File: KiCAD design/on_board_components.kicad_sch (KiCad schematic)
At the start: 11 parts, among them U401 ACS712xLCTR-20A

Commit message: add some comments, connector for battery, bluetooth (is now the PMOD BLE from digikey)
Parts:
- D401: Price 0,35 -> 0.35
- D402, D403: Price 0,36 -> 0.36
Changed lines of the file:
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@@
       (effects (font (size 1.27 1.27)) hide)
     )
-    (property "Price" "0,35" (id 5) (at 133.35 50.8 90)
+    (property "Price" "0.35" (id 5) (at 133.35 50.8 90)
       (effects (font (size 1.27 1.27)) hide)
     )
@@
       (effects (font (size 1.27 1.27)) hide)
     )
-    (property "Price" "0,36" (id 5) (at 162.56 54.61 90)
+    (property "Price" "0.36" (id 5) (at 162.56 54.61 90)
       (effects (font (size 1.27 1.27)) hide)
     )
@@
       (effects (font (size 1.27 1.27)) hide)
     )
-    (property "Price" "0,36" (id 5) (at 176.53 54.61 90)
+    (property "Price" "0.36" (id 5) (at 176.53 54.61 90)
       (effects (font (size 1.27 1.27)) hide)
     )

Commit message: Added capacitors and resistors
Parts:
- C401, C402: footprint Capacitor_SMD:C_0603_1608Metric_Pad1.08x0.95mm_HandSolder -> Capacitor_SMD:C_0805_2012Metric; Price (none) -> 0,09; PurchaseLoc (none) -> https://www.digikey.fi/fi/products/detail/yageo/CC0805KRX7R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
- R404, R405: footprint Resistor_SMD:R_0603_1608Metric_Pad0.98x0.95mm_HandSolder -> Resistor_SMD:R_0805_2012Metric; Price (none) -> 0,09; PurchaseLoc (none) -> https://www.digikey.fi/fi/products/detail/yageo/RC0805FR-07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
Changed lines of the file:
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@@
       (effects (font (size 1.27 1.27)) (justify right))
     )
-    (property "Footprint" "Capacitor_SMD:C_0603_1608Metric_Pad1.08x0.95mm_HandSolder" (id 2) (at 45.4152 31.75 0)
-      (effects (font (size 1.27 1.27)) hide)
-    )
-    (property "Datasheet" "~" (id 3) (at 44.45 35.56 0)
+    (property "Footprint" "Capacitor_SMD:C_0805_2012Metric" (id 2) (at 45.4152 31.75 0)
+      (effects (font (size 1.27 1.27)) hide)
+    )
+    (property "Datasheet" "https://www.yageo.com/upload/media/product/productsearch/datasheet/mlcc/UPY-GPHC_X7R_6.3V-to-250V_22.pdf" (id 3) (at 44.45 35.56 0)
+      (effects (font (size 1.27 1.27)) hide)
+    )
+    (property "PurchaseLoc" "https://www.digikey.fi/fi/products/detail/yageo/CC0805KRX7R9BB104/302874" (id 4) (at 44.45 35.56 0)
+      (effects (font (size 1.27 1.27)) hide)
+    )
+    (property "Price" "0,09" (id 5) (at 44.45 35.56 0)
       (effects (font (size 1.27 1.27)) hide)
     )
@@
       (effects (font (size 1.27 1.27)) (justify right))
     )
-    (property "Footprint" "Capacitor_SMD:C_0603_1608Metric_Pad1.08x0.95mm_HandSolder" (id 2) (at 66.3448 63.5 0)
-      (effects (font (size 1.27 1.27)) hide)
-    )
-    (property "Datasheet" "~" (id 3) (at 67.31 67.31 0)
+    (property "Footprint" "Capacitor_SMD:C_0805_2012Metric" (id 2) (at 66.3448 63.5 0)
+      (effects (font (size 1.27 1.27)) hide)
+    )
+    (property "Datasheet" "https://www.yageo.com/upload/media/product/productsearch/datasheet/mlcc/UPY-GPHC_X7R_6.3V-to-250V_22.pdf" (id 3) (at 67.31 67.31 0)
+      (effects (font (size 1.27 1.27)) hide)
+    )
+    (property "PurchaseLoc" "https://www.digikey.fi/fi/products/detail/yageo/CC0805KRX7R9BB102/302861" (id 4) (at 67.31 67.31 0)
+      (effects (font (size 1.27 1.27)) hide)
+    )
+    (property "Price" "0,09" (id 5) (at 67.31 67.31 0)
       (effects (font (size 1.27 1.27)) hide)
     )
@@
       (effects (font (size 1.27 1.27)) (justify left))
     )
-    (property "Footprint" "Resistor_SMD:R_0603_1608Metric_Pad0.98x0.95mm_HandSolder" (id 2) (at 81.28 60.96 0)
-      (effects (font (size 1.27 1.27)) hide)
-    )
-    (property "Datasheet" "~" (id 3) (at 81.28 60.96 0)
+    (property "Footprint" "Resistor_SMD:R_0805_2012Metric" (id 2) (at 81.28 60.96 0)
+      (effects (font (size 1.27 1.27)) hide)
+    )
+    (property "Datasheet" "https://www.yageo.com/upload/media/product/productsearch/datasheet/rchip/PYu-RC_Group_51_RoHS_L_12.pdf" (id 3) (at 81.28 60.96 0)
+      (effects (font (size 1.27 1.27)) hide)
+    )
+    (property "PurchaseLoc" "https://www.digikey.fi/fi/products/detail/yageo/RC0805FR-071KL/727444" (id 4) (at 81.28 60.96 0)
+      (effects (font (size 1.27 1.27)) hide)
+    )
+    (property "Price" "0,09" (id 5) (at 81.28 60.96 0)
       (effects (font (size 1.27 1.27)) hide)
     )
@@
       (effects (font (size 1.27 1.27)) (justify left))
     )
-    (property "Footprint" "Resistor_SMD:R_0603_1608Metric_Pad0.98x0.95mm_HandSolder" (id 2) (at 81.28 71.12 0)
-      (effects (font (size 1.27 1.27)) hide)
-    )
-    (property "Datasheet" "~" (id 3) (at 81.28 71.12 0)
-      (effects (font (size 1.27 1.27)) hide)
-    )
+    (property "Footprint" "Resistor_SMD:R_0805_2012Metric" (id 2) (at 81.28 71.12 0)
+      (effects (font (size 1.27 1.27)) hide)
+    )
+    (property "Datasheet" "https://www.yageo.com/upload/media/product/productsearch/datasheet/rchip/PYu-RC_Group_51_RoHS_L_12.pdf" (id 3) (at 81.28 71.12 0)
+      (effects (font (size 1.27 1.27)) hide)
+    )
+    (property "PurchaseLoc" "https://www.digikey.fi/fi/products/detail/yageo/RC0805FR-071K91L/727529" (id 4) (at 81.28 71.12 0)
+      (effects (font (size 1.27 1.27)) hide)
+    )
+    (property "Price" "0,09" (id 5) (at 81.28 71.12 0)
+      (effects (font (size 1.27 1.27)) hide)
+    )

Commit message: add link to switch and 1k resistor
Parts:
- R401, R402, R403: Price (none) -> 0.27; PurchaseLoc (none) -> https://www.digikey.fi/fi/products/detail/stackpole-electro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
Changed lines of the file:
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@@
+      (effects (font (size 1.27 1.27)) hide)
+    )
+    (property "Price" "0.27" (id 4) (at 176.53 62.23 0)
+      (effects (font (size 1.27 1.27)) hide)
+    )
+    (property "PurchaseLoc" "https://www.digikey.fi/fi/products/detail/stackpole-electronics-inc/RNCP0805FTD1K00/2240229" (id 5) (at 176.53 62.23 0)
       (effects (font (size 1.27 1.27)) hide)
     )
@@
       (effects (font (size 1.27 1.27)) hide)
     )
+    (property "Price" "0.27" (id 4) (at 162.56 62.23 0)
+      (effects (font (size 1.27 1.27)) hide)
+    )
+    (property "PurchaseLoc" "https://www.digikey.fi/fi/products/detail/stackpole-electronics-inc/RNCP0805FTD1K00/2240229" (id 5) (at 162.56 62.23 0)
+      (effects (font (size 1.27 1.27)) hide)
+    )
     (pin "1")
     (pin "2")
@@
       (effects (font (size 1.27 1.27)) hide)
     )
+    (property "Price" "0.27" (id 4) (at 133.35 58.42 0)
+      (effects (font (size 1.27 1.27)) hide)
+    )
+    (property "PurchaseLoc" "https://www.digikey.fi/fi/products/detail/stackpole-electronics-inc/RNCP0805FTD1K00/2240229" (id 5) (at 133.35 58.42 0)
+      (effects (font (size 1.27 1.27)) hide)
+    )

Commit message: use . as decimal separator
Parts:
- C401, C402, R404, R405: Price 0,09 -> 0.09
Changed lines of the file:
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@@
       (effects (font (size 1.27 1.27)) hide)
     )
-    (property "Price" "0,09" (id 5) (at 44.45 35.56 0)
+    (property "Price" "0.09" (id 5) (at 44.45 35.56 0)
       (effects (font (size 1.27 1.27)) hide)
     )
@@
       (effects (font (size 1.27 1.27)) hide)
     )
-    (property "Price" "0,09" (id 5) (at 67.31 67.31 0)
+    (property "Price" "0.09" (id 5) (at 67.31 67.31 0)
       (effects (font (size 1.27 1.27)) hide)
     )
@@
       (effects (font (size 1.27 1.27)) hide)
     )
-    (property "Price" "0,09" (id 5) (at 81.28 60.96 0)
+    (property "Price" "0.09" (id 5) (at 81.28 60.96 0)
       (effects (font (size 1.27 1.27)) hide)
     )
@@
       (effects (font (size 1.27 1.27)) hide)
     )
-    (property "Price" "0,09" (id 5) (at 81.28 71.12 0)
-      (effects (font (size 1.27 1.27)) hide)
-    )
+    (property "Price" "0.09" (id 5) (at 81.28 71.12 0)
+      (effects (font (size 1.27 1.27)) hide)
+    )

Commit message: Fixed info of 3 resistors in LED sheet
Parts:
- R401, R402, R403: footprint Resistor_SMD:R_0603_1608Metric_Pad0.98x0.95mm_HandSolder -> Resistor_SMD:R_0805_2012Metric; Price 0.27 -> 0.09; PurchaseLoc https://www.digikey.fi/fi/products/detail/stackpole-electro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 -> https://www.digikey.fi/fi/products/detail/yageo/RC0805FR-07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
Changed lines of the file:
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@@
       (effects (font (size 1.27 1.27)) (justify left))
     )
-    (property "Footprint" "Resistor_SMD:R_0603_1608Metric_Pad0.98x0.95mm_HandSolder" (id 2) (at 176.53 62.23 0)
-      (effects (font (size 1.27 1.27)) hide)
-    )
-    (property "Datasheet" "~" (id 3) (at 176.53 62.23 0)
-      (effects (font (size 1.27 1.27)) hide)
-    )
-    (property "Price" "0.27" (id 4) (at 176.53 62.23 0)
-      (effects (font (size 1.27 1.27)) hide)
-    )
-    (property "PurchaseLoc" "https://www.digikey.fi/fi/products/detail/stackpole-electronics-inc/RNCP0805FTD1K00/2240229" (id 5) (at 176.53 62.23 0)
+    (property "Footprint" "Resistor_SMD:R_0805_2012Metric" (id 2) (at 176.53 62.23 0)
+      (effects (font (size 1.27 1.27)) hide)
+    )
+    (property "Datasheet" "https://www.yageo.com/upload/media/product/productsearch/datasheet/rchip/PYu-RC_Group_51_RoHS_L_12.pdf" (id 3) (at 176.53 62.23 0)
+      (effects (font (size 1.27 1.27)) hide)
+    )
+    (property "Price" "0.09" (id 4) (at 176.53 62.23 0)
+      (effects (font (size 1.27 1.27)) hide)
+    )
+    (property "PurchaseLoc" "https://www.digikey.fi/fi/products/detail/yageo/RC0805FR-071KL/727444" (id 5) (at 176.53 62.23 0)
       (effects (font (size 1.27 1.27)) hide)
     )
@@
       (effects (font (size 1.27 1.27)) (justify left))
     )
-    (property "Footprint" "Resistor_SMD:R_0603_1608Metric_Pad0.98x0.95mm_HandSolder" (id 2) (at 162.56 62.23 0)
-      (effects (font (size 1.27 1.27)) hide)
-    )
-    (property "Datasheet" "~" (id 3) (at 162.56 62.23 0)
-      (effects (font (size 1.27 1.27)) hide)
-    )
-    (property "Price" "0.27" (id 4) (at 162.56 62.23 0)
-      (effects (font (size 1.27 1.27)) hide)
-    )
-    (property "PurchaseLoc" "https://www.digikey.fi/fi/products/detail/stackpole-electronics-inc/RNCP0805FTD1K00/2240229" (id 5) (at 162.56 62.23 0)
+    (property "Footprint" "Resistor_SMD:R_0805_2012Metric" (id 2) (at 162.56 62.23 0)
+      (effects (font (size 1.27 1.27)) hide)
+    )
+    (property "Datasheet" "https://www.yageo.com/upload/media/product/productsearch/datasheet/rchip/PYu-RC_Group_51_RoHS_L_12.pdf" (id 3) (at 162.56 62.23 0)
+      (effects (font (size 1.27 1.27)) hide)
+    )
+    (property "Price" "0.09" (id 4) (at 162.56 62.23 0)
+      (effects (font (size 1.27 1.27)) hide)
+    )
+    (property "PurchaseLoc" "https://www.digikey.fi/fi/products/detail/yageo/RC0805FR-071KL/727444" (id 5) (at 162.56 62.23 0)
       (effects (font (size 1.27 1.27)) hide)
     )
@@
       (effects (font (size 1.27 1.27)) (justify left))
     )
-    (property "Footprint" "Resistor_SMD:R_0603_1608Metric_Pad0.98x0.95mm_HandSolder" (id 2) (at 133.35 58.42 0)
-      (effects (font (size 1.27 1.27)) hide)
-    )
-    (property "Datasheet" "~" (id 3) (at 133.35 58.42 0)
-      (effects (font (size 1.27 1.27)) hide)
-    )
-    (property "Price" "0.27" (id 4) (at 133.35 58.42 0)
-      (effects (font (size 1.27 1.27)) hide)
-    )
-    (property "PurchaseLoc" "https://www.digikey.fi/fi/products/detail/stackpole-electronics-inc/RNCP0805FTD1K00/2240229" (id 5) (at 133.35 58.42 0)
-      (effects (font (size 1.27 1.27)) hide)
-    )
+    (property "Footprint" "Resistor_SMD:R_0805_2012Metric" (id 2) (at 133.35 58.42 0)
+      (effects (font (size 1.27 1.27)) hide)
+    )
+    (property "Datasheet" "https://www.yageo.com/upload/media/product/productsearch/datasheet/rchip/PYu-RC_Group_51_RoHS_L_12.pdf" (id 3) (at 133.35 58.42 0)
+      (effects (font (size 1.27 1.27)) hide)
+    )
+    (property "Price" "0.09" (id 4) (at 133.35 58.42 0)
+      (effects (font (size 1.27 1.27)) hide)
+    )
+    (property "PurchaseLoc" "https://www.digikey.fi/fi/products/detail/yageo/RC0805FR-071KL/727444" (id 5) (at 133.35 58.42 0)
+      (effects (font (size 1.27 1.27)) hide)
+    )

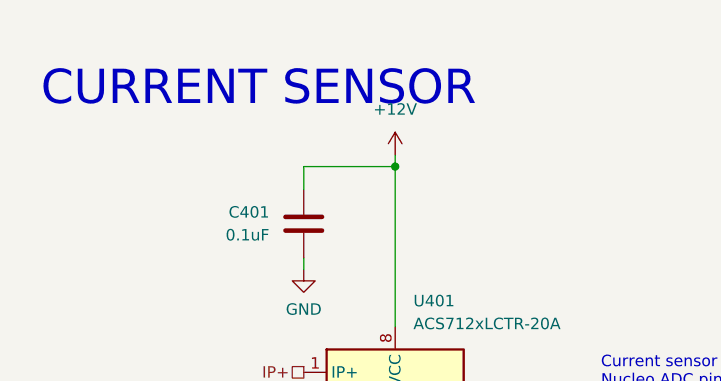
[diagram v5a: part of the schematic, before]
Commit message: current sensor VCC should be 5V
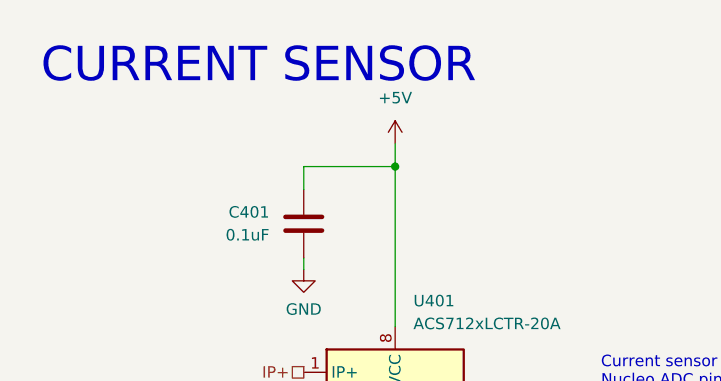
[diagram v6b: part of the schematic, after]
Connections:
- net +12V: no longer C401.2, U401.8 (VCC)
- new net +5V: C401.2, U401.8 (VCC)
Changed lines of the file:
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@@
     (stroke (width 0) (type default) (color 0 0 0 0))
   )
-  (wire (pts (xy 54.61 27.94) (xy 54.61 29.21))
+  (wire (pts (xy 54.61 26.67) (xy 54.61 29.21))
     (stroke (width 0) (type default) (color 0 0 0 0))
   )
@@
     (effects (font (size 1.27 1.27)) (justify left bottom))
   )
-  (text "CURRENT SENSOR\n" (at 15.24 22.86 0)
+  (text "CURRENT SENSOR\n" (at 15.24 20.32 0)
     (effects (font (size 3.81 3.81)) (justify left bottom))
   )
@@
     (pin "1")
     (pin "2")
-  )
-  (symbol (lib_id "power:+12V") (at 54.61 27.94 0) (unit 1)
-    (in_bom yes) (on_board yes) (fields_autoplaced)
-    (property "Reference" "#PWR0111" (id 0) (at 54.61 31.75 0)
-      (effects (font (size 1.27 1.27)) hide)
-    )
-    (property "Value" "+12V" (id 1) (at 54.61 22.86 0))
-    (property "Footprint" "" (id 2) (at 54.61 27.94 0)
-      (effects (font (size 1.27 1.27)) hide)
-    )
-    (property "Datasheet" "" (id 3) (at 54.61 27.94 0)
-      (effects (font (size 1.27 1.27)) hide)
-    )
-    (pin "1")
   )
   (symbol (lib_id "Device:C") (at 67.31 67.31 180) (unit 1)
@@
       (effects (font (size 1.27 1.27)) hide)
     )
+    (pin "1")
+  )
+  (symbol (lib_id "power:+5V") (at 54.61 26.67 0) (unit 1)
+    (in_bom yes) (on_board yes) (fields_autoplaced)
+    (property "Reference" "#PWR?" (id 0) (at 54.61 30.48 0)
+      (effects (font (size 1.27 1.27)) hide)
+    )
+    (property "Value" "+5V" (id 1) (at 54.61 21.59 0))
+    (property "Footprint" "" (id 2) (at 54.61 26.67 0)
+      (effects (font (size 1.27 1.27)) hide)
+    )
+    (property "Datasheet" "" (id 3) (at 54.61 26.67 0)
+      (effects (font (size 1.27 1.27)) hide)
+    )

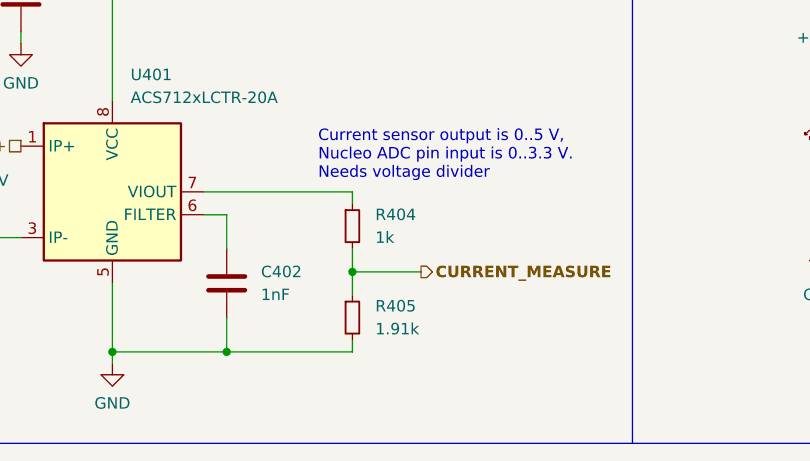
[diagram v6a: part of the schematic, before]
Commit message: 10x larger resistors for voltage divider
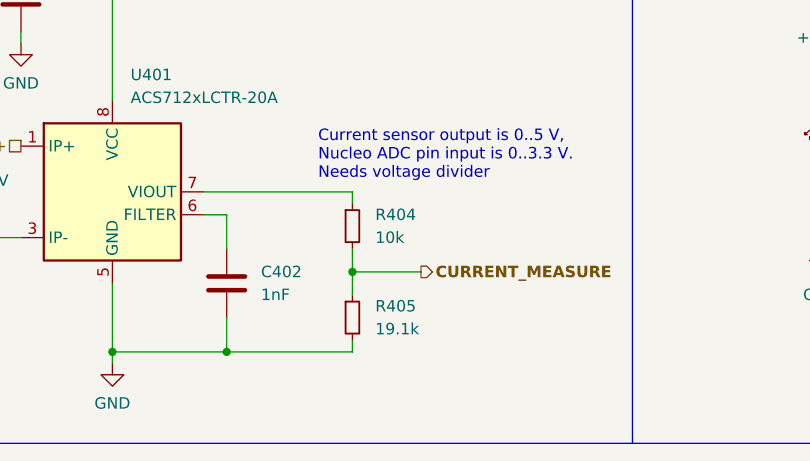
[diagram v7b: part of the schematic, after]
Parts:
- R404: value 1k -> 10k; PurchaseLoc https://www.digikey.fi/fi/products/detail/yageo/RC0805FR-07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 -> https://www.digikey.fi/en/products/detail/yageo/AC0402FR-07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
- R405: value 1.91k -> 19.1k; PurchaseLoc https://www.digikey.fi/fi/products/detail/yageo/RC0805FR-07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 -> https://www.digikey.fi/en/products/detail/yageo/AC0402FR-07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
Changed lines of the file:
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@@
       (effects (font (size 1.27 1.27)) (justify left))
     )
-    (property "Value" "1k" (id 1) (at 83.82 62.2299 0)
+    (property "Value" "10k" (id 1) (at 83.82 62.2299 0)
       (effects (font (size 1.27 1.27)) (justify left))
     )
@@
       (effects (font (size 1.27 1.27)) hide)
     )
-    (property "PurchaseLoc" "https://www.digikey.fi/fi/products/detail/yageo/RC0805FR-071KL/727444" (id 4) (at 81.28 60.96 0)
+    (property "PurchaseLoc" "https://www.digikey.fi/en/products/detail/yageo/AC0402FR-0710KL/5895030" (id 4) (at 81.28 60.96 0)
       (effects (font (size 1.27 1.27)) hide)
     )
@@
       (effects (font (size 1.27 1.27)) (justify left))
     )
-    (property "Value" "1.91k" (id 1) (at 83.82 72.3899 0)
+    (property "Value" "19.1k" (id 1) (at 83.82 72.3899 0)
       (effects (font (size 1.27 1.27)) (justify left))
     )
@@
       (effects (font (size 1.27 1.27)) hide)
     )
-    (property "PurchaseLoc" "https://www.digikey.fi/fi/products/detail/yageo/RC0805FR-071K91L/727529" (id 4) (at 81.28 71.12 0)
-      (effects (font (size 1.27 1.27)) hide)
-    )
+    (property "PurchaseLoc" "https://www.digikey.fi/en/products/detail/yageo/AC0402FR-0719K1L/5895123" (id 4) (at 81.28 71.12 0)
+      (effects (font (size 1.27 1.27)) hide)
+    )

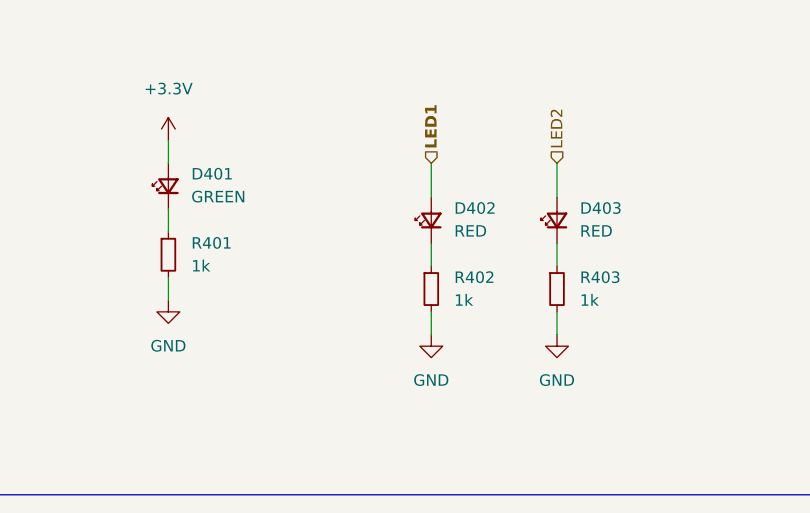
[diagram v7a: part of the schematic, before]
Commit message: change led resistors to 330 ohm
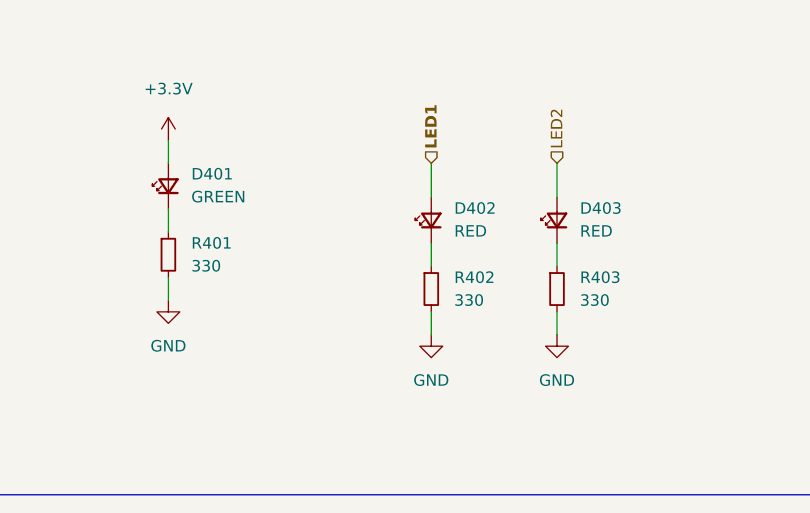
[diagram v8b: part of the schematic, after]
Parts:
- R401, R402, R403: value 1k -> 330; PurchaseLoc https://www.digikey.fi/fi/products/detail/yageo/RC0805FR-07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 -> https://www.digikey.fi/en/products/detail/yageo/Rc0805Jr-07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
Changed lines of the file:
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@@
       (effects (font (size 1.27 1.27)) (justify left))
     )
-    (property "Value" "1k" (id 1) (at 179.07 63.4999 0)
+    (property "Value" "330" (id 1) (at 179.07 63.4999 0)
       (effects (font (size 1.27 1.27)) (justify left))
     )
@@
       (effects (font (size 1.27 1.27)) hide)
     )
-    (property "PurchaseLoc" "https://www.digikey.fi/fi/products/detail/yageo/RC0805FR-071KL/727444" (id 5) (at 176.53 62.23 0)
+    (property "PurchaseLoc" "https://www.digikey.fi/en/products/detail/yageo/Rc0805Jr-07330RL/728311" (id 5) (at 176.53 62.23 0)
       (effects (font (size 1.27 1.27)) hide)
     )
@@
       (effects (font (size 1.27 1.27)) (justify left))
     )
-    (property "Value" "1k" (id 1) (at 165.1 63.4999 0)
+    (property "Value" "330" (id 1) (at 165.1 63.4999 0)
       (effects (font (size 1.27 1.27)) (justify left))
     )
@@
       (effects (font (size 1.27 1.27)) hide)
     )
-    (property "PurchaseLoc" "https://www.digikey.fi/fi/products/detail/yageo/RC0805FR-071KL/727444" (id 5) (at 162.56 62.23 0)
+    (property "PurchaseLoc" "https://www.digikey.fi/en/products/detail/yageo/Rc0805Jr-07330RL/728311" (id 5) (at 162.56 62.23 0)
       (effects (font (size 1.27 1.27)) hide)
     )
@@
       (effects (font (size 1.27 1.27)) (justify left))
     )
-    (property "Value" "1k" (id 1) (at 135.89 59.6899 0)
+    (property "Value" "330" (id 1) (at 135.89 59.6899 0)
       (effects (font (size 1.27 1.27)) (justify left))
     )
@@
       (effects (font (size 1.27 1.27)) hide)
     )
-    (property "PurchaseLoc" "https://www.digikey.fi/fi/products/detail/yageo/RC0805FR-071KL/727444" (id 5) (at 133.35 58.42 0)
-      (effects (font (size 1.27 1.27)) hide)
-    )
+    (property "PurchaseLoc" "https://www.digikey.fi/en/products/detail/yageo/Rc0805Jr-07330RL/728311" (id 5) (at 133.35 58.42 0)
+      (effects (font (size 1.27 1.27)) hide)
+    )
